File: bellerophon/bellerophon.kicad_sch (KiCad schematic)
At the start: 16 parts, among them Q1 IRLB8721PBF

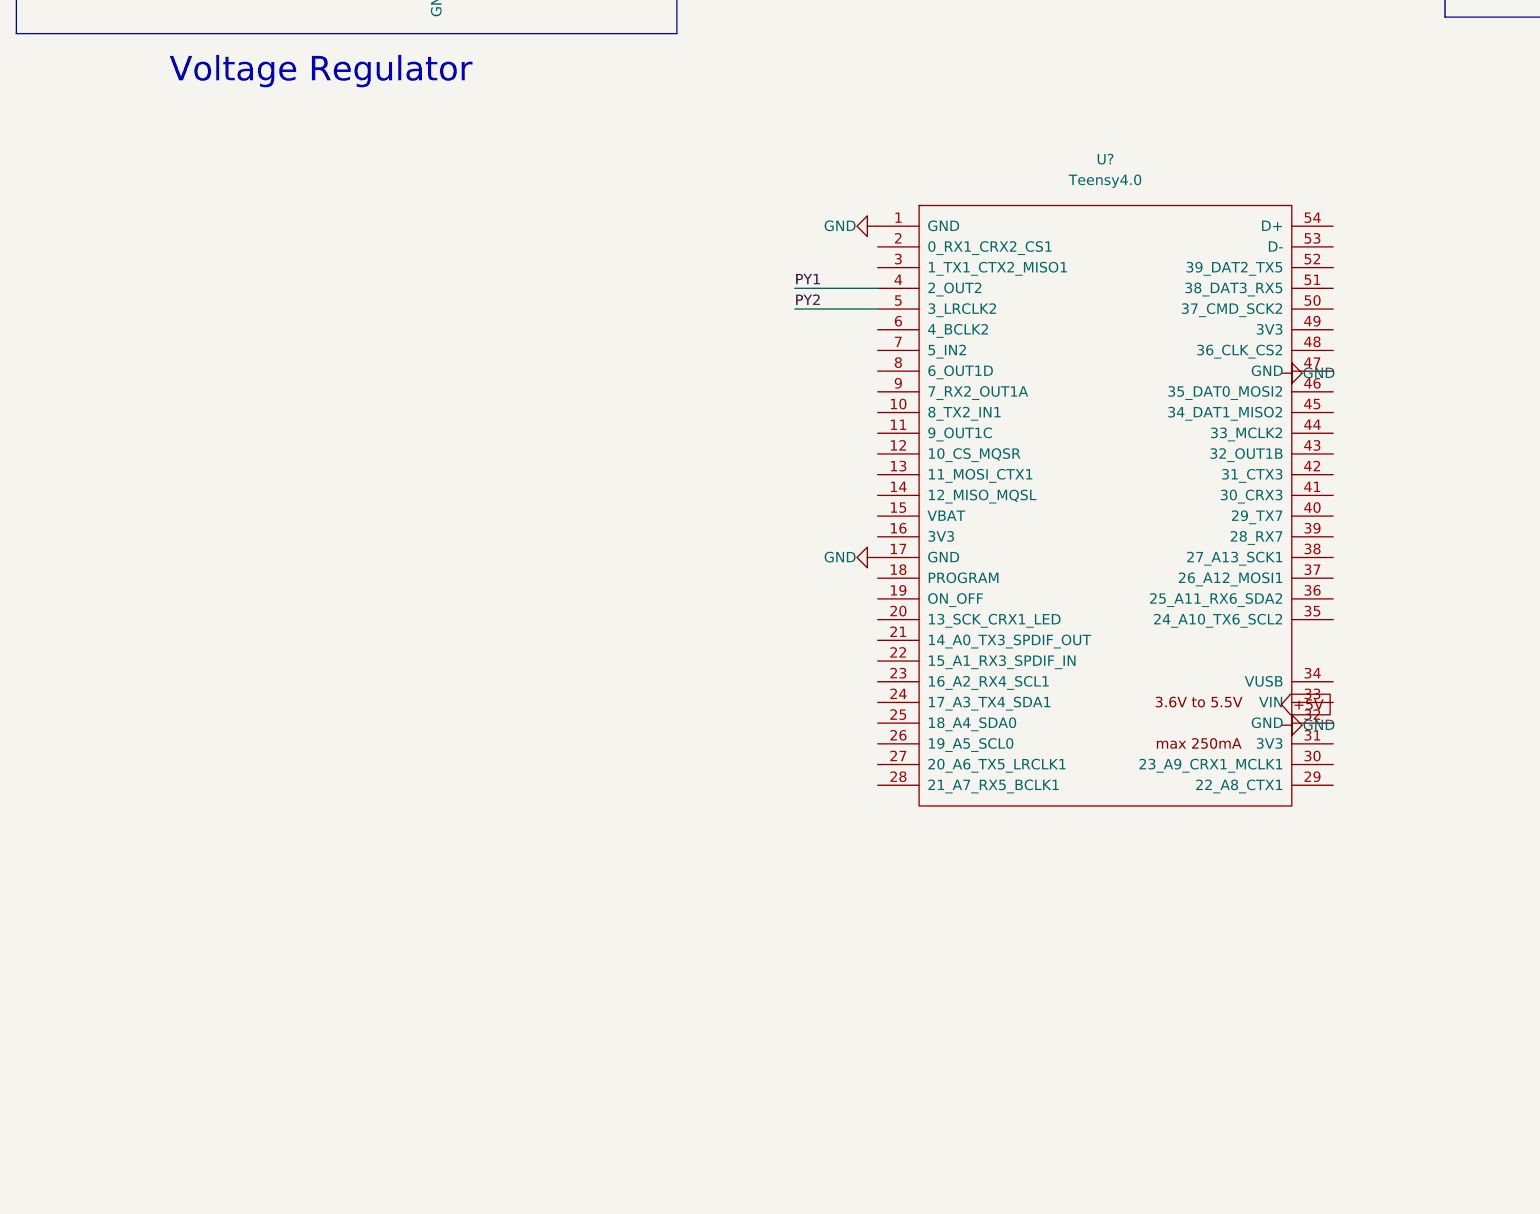
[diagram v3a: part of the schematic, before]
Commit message: LED/Buzzer circuits added to bellerophon schematic
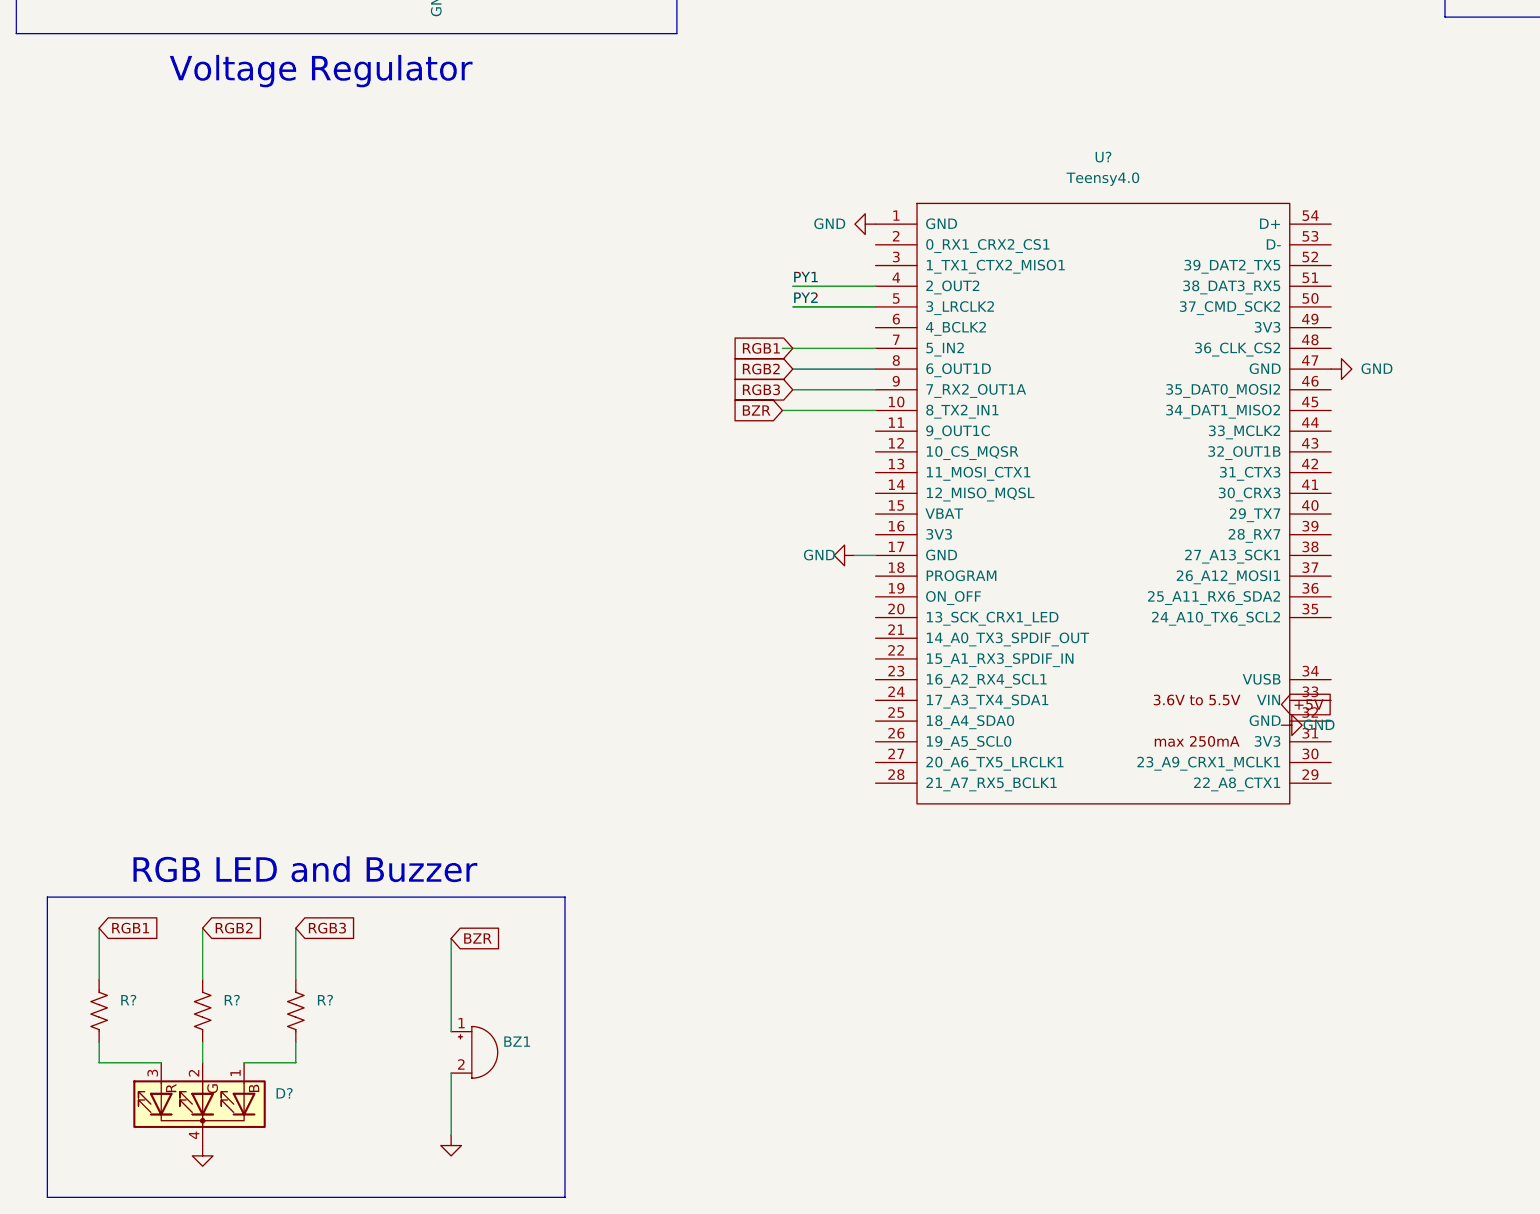
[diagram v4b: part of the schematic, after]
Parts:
- added BZ1: (no value), symbol Device:Buzzer
- added D?: (no value), symbol Device:LED_BGRK
- added R? (x3): (no value), symbol Device:R_US
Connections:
- net GND: now also U?.47 (GND), BZ1.2 (+), D?.4 (K)
- net BZR: now reaches U?.10 (8_TX2_IN1)
- net BZR: now also BZ1.1 (-)
- net RGB1: now reaches U?.7 (5_IN2)
- net RGB1: now also R?.1
- net RGB2: now reaches U?.8 (6_OUT1D)
- net RGB2: now also R?.1
- net RGB3: now reaches U?.9 (7_RX2_OUT1A)
- net RGB3: now also R?.1
- new net: D?.1 (BA), R?.2
- new net: D?.3 (RA), R?.2
- new net: D?.2 (GA), R?.2
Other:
- note added: "RGB LED and Buzzer"

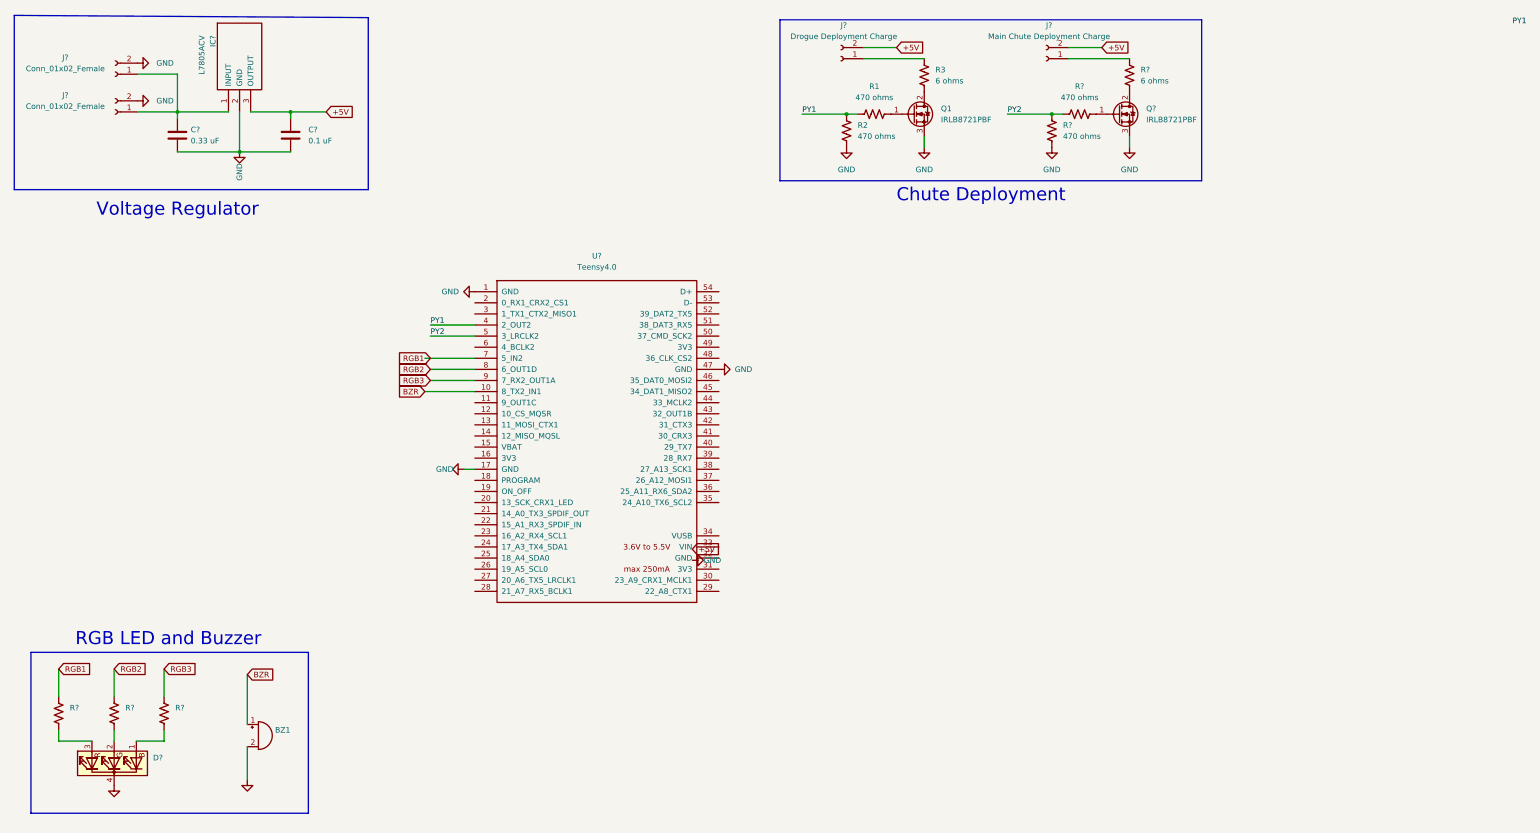
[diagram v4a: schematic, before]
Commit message: PaulBess: added drawing for Adafruit MPL3115A2, goldenjinjo: changed chute deployment resistors to 5 ohms
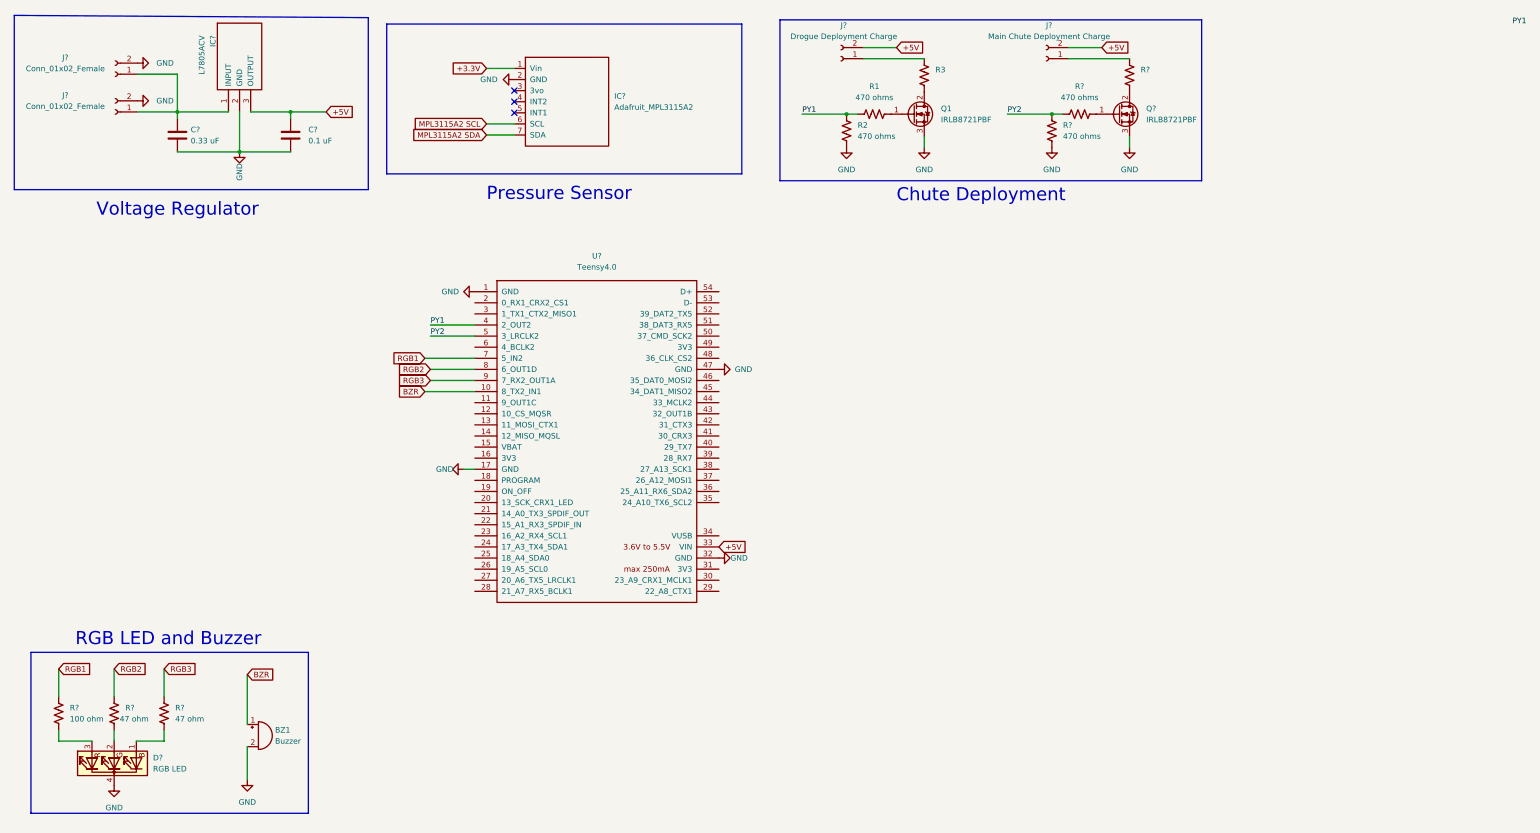
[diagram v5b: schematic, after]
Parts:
- added IC?: Adafruit_MPL3115A2, Adafruit_MPL3115A2:1x07, symbol Adafruit:Adafruit_MPL3115A2
- BZ1: value (none) -> Buzzer
- D?: value (none) -> RGB LED
- R3, R?: value 6 ohms -> (none)
- R? (x2): value (none) -> 47 ohm
- R?: value (none) -> 100 ohm
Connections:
- net +5V: now also U?.33 (VIN)
- net GND: now also U?.32 (GND), IC?.2 (GND)
- new net +3.3V: IC?.1 (Vin)
- new net MPL3115A2 SCL: IC?.6 (SCL)
- new net MPL3115A2 SDA: IC?.7 (SDA)
- no-connect marks 0 -> 3
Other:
- note added: "Pressure Sensor"

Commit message: fixed misalignment on SD chip symbol; added SD chip drawing to schematic
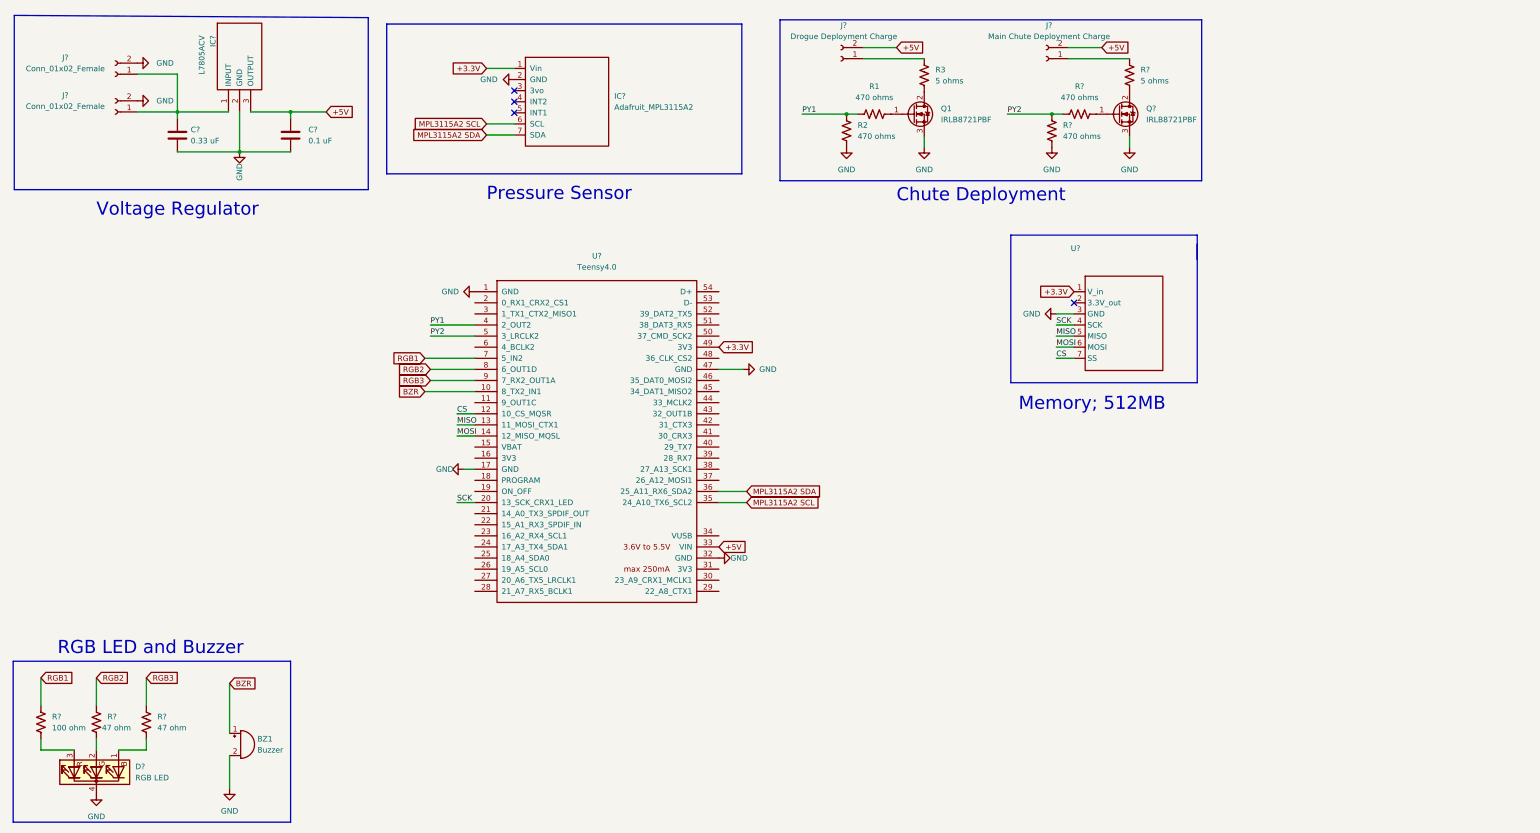
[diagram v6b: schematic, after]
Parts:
- added U?: (no value), symbol Adafruit:Adafruit SPI Flash SD Card
- R3, R?: value (none) -> 5 ohms
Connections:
- net +3.3V: now also U?.49 (3V3), U?.1 (V_in)
- net GND: now also U?.3 (GND)
- net MPL3115A2 SCL: now also U?.35 (24_A10_TX6_SCL2)
- net MPL3115A2 SDA: now also U?.36 (25_A11_RX6_SDA2)
- net CS: now reaches U?.12 (10_CS_MQSR)
- net CS: now also U?.7 (SS)
- net MISO: now reaches U?.13 (11_MOSI_CTX1)
- net MISO: now also U?.5 (MISO)
- net MOSI: now reaches U?.14 (12_MISO_MQSL)
- net MOSI: now also U?.6 (MOSI)
- net SCK: now reaches U?.20 (13_SCK_CRX1_LED)
- net SCK: now also U?.4 (SCK)
- no-connect marks 3 -> 4
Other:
- note added: "Memory; 512MB"
- moved on the sheet: BZ1, D?, R?

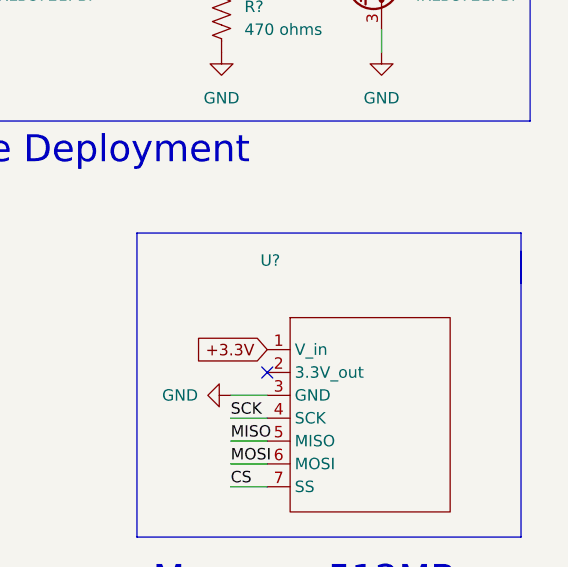
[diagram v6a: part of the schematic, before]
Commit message: improved dimensional accuracy of MPL3115A2 footprint
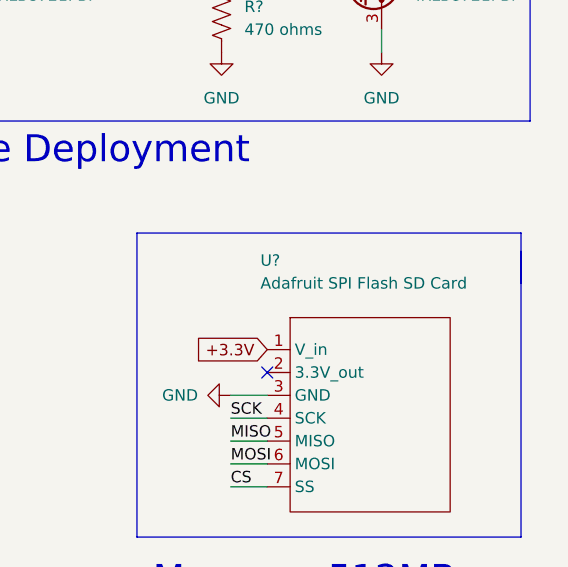
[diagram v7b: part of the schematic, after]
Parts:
- IC?: footprint Adafruit_MPL3115A2:1x07 -> Adafruit:MPL3115A2-B19.05x17.78mm-1x07-P2.54mm
- U?: value (none) -> Adafruit SPI Flash SD Card; footprint (none) -> Adafruit:SD-CARD-B21.59x17.78mm-1X07_ROUND_70-P2.5mm
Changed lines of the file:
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@@
       (effects (font (size 1.27 1.27)) (justify left))
     )
-    (property "Footprint" "Adafruit_MPL3115A2:1x07" (id 2) (at 141.1224 32.7152 0)
+    (property "Footprint" "Adafruit:MPL3115A2-B19.05x17.78mm-1x07-P2.54mm" (id 2) (at 141.1224 32.7152 0)
       (effects (font (size 1.27 1.27)) hide)
     )
@@
       (effects (font (size 1.27 1.27)) (justify left))
     )
-    (property "Value" "" (id 1) (at 254.508 68.834 90)
-      (effects (font (size 1.27 1.27)) (justify left))
-    )
-    (property "Footprint" "" (id 2) (at 261.9248 72.7964 0)
+    (property "Value" "Adafruit SPI Flash SD Card" (id 1) (at 254.508 68.834 90)
+      (effects (font (size 1.27 1.27)) (justify left))
+    )
+    (property "Footprint" "Adafruit:SD-CARD-B21.59x17.78mm-1X07_ROUND_70-P2.5mm" (id 2) (at 261.9248 72.7964 0)
       (effects (font (size 1.27 1.27)) hide)
     )
@@
     )
     (path "/48d05432-6f02-424e-bb3b-de7569cfe224"
-      (reference "IC?") (unit 1) (value "Adafruit_MPL3115A2") (footprint "Adafruit_MPL3115A2:1x07")
+      (reference "IC?") (unit 1) (value "Adafruit_MPL3115A2") (footprint "Adafruit:MPL3115A2-B19.05x17.78mm-1x07-P2.54mm")
     )
     (path "/271396f2-2847-47d1-bb55-41a773d0e0d6"
